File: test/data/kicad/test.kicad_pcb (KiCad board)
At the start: 2 copper layers, 101.6 x 53.3 mm, 64 parts, among them IC2 ATMEGA1280-16AU, IC4 MC33269D-5.0, IC6 FT232RL, IC7 LM358D, Q2 16MHz, T1 NDT2955, X2 DC21MMX

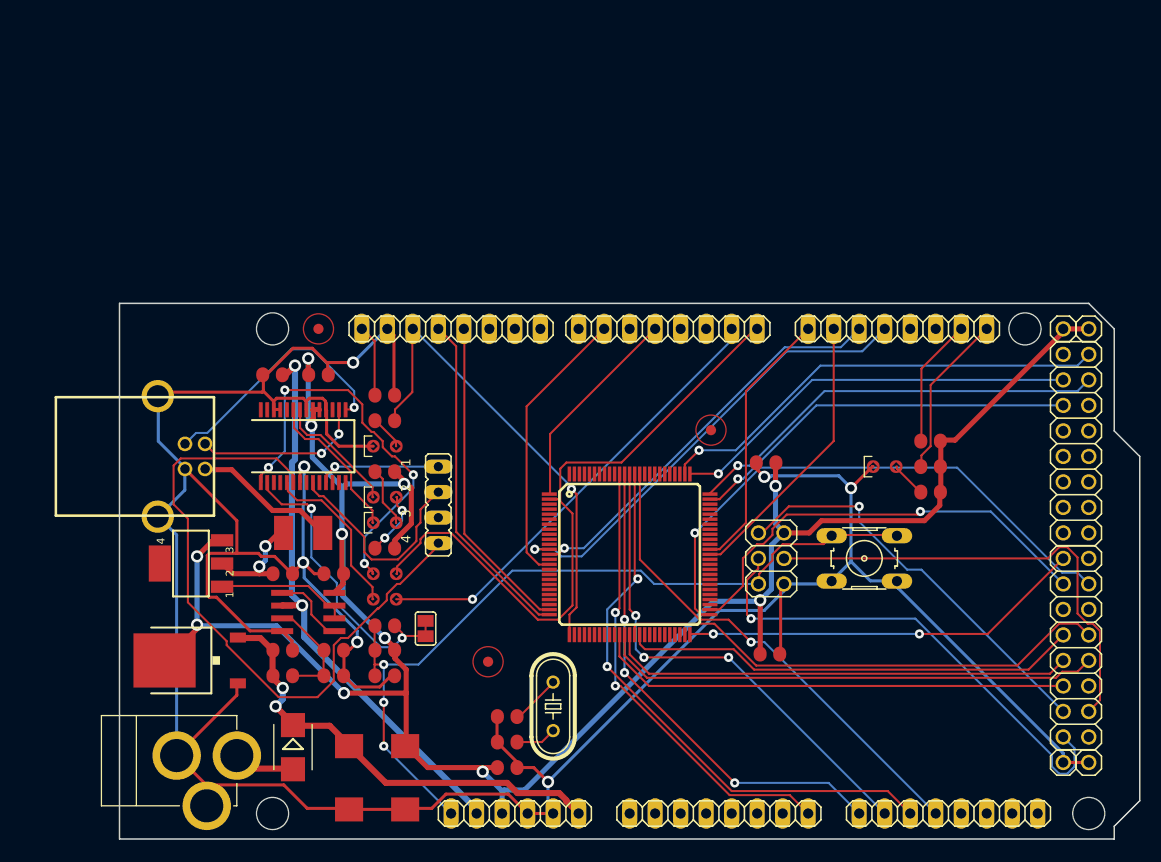
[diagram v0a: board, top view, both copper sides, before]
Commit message: rftr: kicad parser
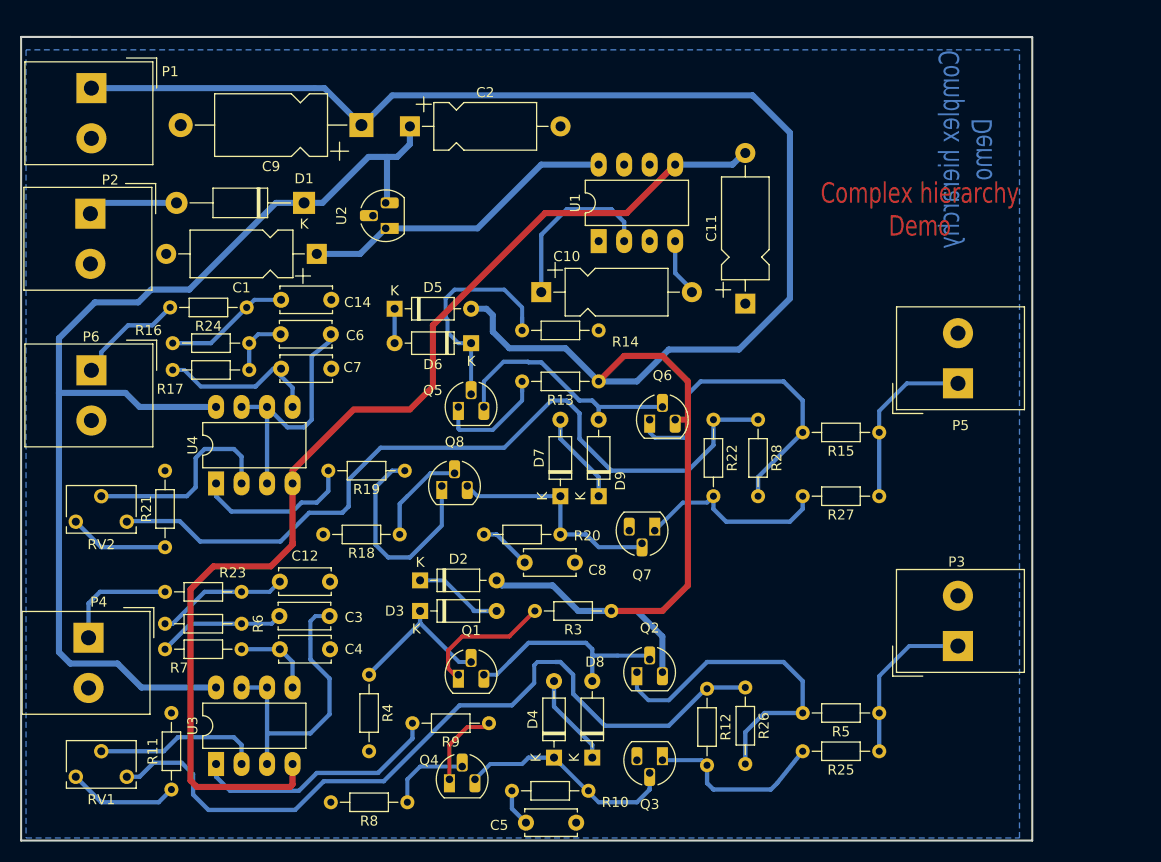
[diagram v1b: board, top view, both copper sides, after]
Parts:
- removed @HOLE0, @HOLE1, @HOLE2, @HOLE3: , 
- removed ADCH, ADCL, COMMUNICATION, PWMH, PWML: , 1X08
- removed C13, C15, C16, C17: 100n, C0805RND
- removed F1: 500mA, L1812
- removed IC2: ATMEGA1280-16AU, TQFP100
- removed IC4: MC33269D-5.0, DPACK
- removed IC6: FT232RL, SSOP28
- removed IC7: LM358D, SO08
- removed ICSP: ICSP, 2X03
- removed JP1, JP2: , 2X08
- removed JP3, JP4, JP5, JP6: , 1X01
- removed L, PWR, RX, TX: , 0805RND
- removed POWER: , 1X06
- removed R1: 1K, R0805RND
- removed R2: 10k, R0805RND
- removed RESET-EN: , SJ
- removed S1: , B3F-10XX
- removed T1: NDT2955, SOT223
- removed U$1, U$2, U$3: FIDUCIALMOUNT, FIDUCIA-MOUNT
- removed X2: DC21MMX, DC-21MM
- removed X3: , JP4
- removed X4: , PN61729
- added C8: 820pF, Capacitor_THT:C_Disc_D5.0mm_W2.5mm_P5.00mm, F.Cu at (138.0, 104.1)
- added D2: 1N4148, Diode_THT:D_DO-35_SOD27_P7.62mm_Horizontal, F.Cu at (127.6, 105.9)
- added D3: 1N4148, Diode_THT:D_DO-35_SOD27_P7.62mm_Horizontal, F.Cu at (127.6, 109.0)
- added D4: 1N4148, Diode_THT:D_DO-35_SOD27_P7.62mm_Horizontal, F.Cu at (141.0, 123.6)
- added D5: 1N4148, Diode_THT:D_DO-35_SOD27_P7.62mm_Horizontal, F.Cu at (125.1, 78.9)
- added D6: 1N4148, Diode_THT:D_DO-35_SOD27_P7.62mm_Horizontal, F.Cu at (132.7, 82.3)
- added D7: 1N4148, Diode_THT:D_DO-35_SOD27_P7.62mm_Horizontal, F.Cu at (141.6, 97.5)
- added D8: 1N4148, Diode_THT:D_DO-35_SOD27_P7.62mm_Horizontal, F.Cu at (144.8, 123.6)
- added D9: 1N4148, Diode_THT:D_DO-35_SOD27_P7.62mm_Horizontal, F.Cu at (145.4, 97.5)
- added P1: CONN_2, TerminalBlock_Altech:Altech_AK300_1x02_P5.00mm_45-Degree, F.Cu at (94.9, 56.9)
- added P2: CONN_2, TerminalBlock_Altech:Altech_AK300_1x02_P5.00mm_45-Degree, F.Cu at (94.8, 69.4)
- added P3: CONN_2, TerminalBlock_Altech:Altech_AK300_1x02_P5.00mm_45-Degree, F.Cu at (181.2, 112.5)
- added P4: CONN_2, TerminalBlock_Altech:Altech_AK300_1x02_P5.00mm_45-Degree, F.Cu at (94.6, 111.6)
- added P5: CONN_2, TerminalBlock_Altech:Altech_AK300_1x02_P5.00mm_45-Degree, F.Cu at (181.2, 86.3)
- added P6: CONN_2, TerminalBlock_Altech:Altech_AK300_1x02_P5.00mm_45-Degree, F.Cu at (94.9, 85.0)
- added Q1: MPSA92, Package_TO_SOT_THT:TO-92_HandSolder, F.Cu at (131.4, 115.3)
- added Q3: MPSA92, Package_TO_SOT_THT:TO-92_HandSolder, F.Cu at (151.8, 123.8)
- added Q4: MPSA42, Package_TO_SOT_THT:TO-92_HandSolder, F.Cu at (130.6, 125.7)
- added Q5: MPSA92, Package_TO_SOT_THT:TO-92_HandSolder, F.Cu at (131.4, 88.6)
- added Q6: MPSA42, Package_TO_SOT_THT:TO-92_HandSolder, F.Cu at (150.5, 89.9)
- added Q7: MPSA92, Package_TO_SOT_THT:TO-92_HandSolder, F.Cu at (151.0, 101.0)
- added Q8: MPSA42, Package_TO_SOT_THT:TO-92_HandSolder, F.Cu at (129.8, 96.5)
- added R13: 470, Resistor_THT:R_Axial_DIN0204_L3.6mm_D1.6mm_P7.62mm_Horizontal, F.Cu at (145.4, 86.1)
- added R14: 220K, Resistor_THT:R_Axial_DIN0204_L3.6mm_D1.6mm_P7.62mm_Horizontal, F.Cu at (137.8, 81.0)
- added R15: 47, Resistor_THT:R_Axial_DIN0204_L3.6mm_D1.6mm_P7.62mm_Horizontal, F.Cu at (173.4, 91.2)
- added R16: 22K, Resistor_THT:R_Axial_DIN0204_L3.6mm_D1.6mm_P7.62mm_Horizontal, F.Cu at (110.6, 82.3)
- added R17: 22K, Resistor_THT:R_Axial_DIN0204_L3.6mm_D1.6mm_P7.62mm_Horizontal, F.Cu at (103.0, 85.0)
- added R18: 1K, Resistor_THT:R_Axial_DIN0204_L3.6mm_D1.6mm_P7.62mm_Horizontal, F.Cu at (125.6, 101.3)
- added R19: 1K, Resistor_THT:R_Axial_DIN0204_L3.6mm_D1.6mm_P7.62mm_Horizontal, F.Cu at (126.1, 95.0)
- added R20: 5,6K, Resistor_THT:R_Axial_DIN0204_L3.6mm_D1.6mm_P7.62mm_Horizontal, F.Cu at (141.6, 101.3)
- added R21: 4,7K, Resistor_THT:R_Axial_DIN0204_L3.6mm_D1.6mm_P7.62mm_Horizontal, F.Cu at (102.2, 102.6)
- added R22: 220K, Resistor_THT:R_Axial_DIN0204_L3.6mm_D1.6mm_P7.62mm_Horizontal, F.Cu at (156.8, 89.9)
- added R23: 1K, Resistor_THT:R_Axial_DIN0204_L3.6mm_D1.6mm_P7.62mm_Horizontal, F.Cu at (109.9, 107.1)
- added R24: 1K, Resistor_THT:R_Axial_DIN0204_L3.6mm_D1.6mm_P7.62mm_Horizontal, F.Cu at (110.4, 78.7)
- added R25: 47, Resistor_THT:R_Axial_DIN0204_L3.6mm_D1.6mm_P7.62mm_Horizontal, F.Cu at (173.4, 122.9)
- added R26: 220K, Resistor_THT:R_Axial_DIN0204_L3.6mm_D1.6mm_P7.62mm_Horizontal, F.Cu at (160.0, 116.6)
- added R27: 47, Resistor_THT:R_Axial_DIN0204_L3.6mm_D1.6mm_P7.62mm_Horizontal, F.Cu at (173.4, 97.5)
- added R28: 220K, Resistor_THT:R_Axial_DIN0204_L3.6mm_D1.6mm_P7.62mm_Horizontal, F.Cu at (161.3, 89.9)
- added R4: 220K, Resistor_THT:R_Axial_DIN0204_L3.6mm_D1.6mm_P7.62mm_Horizontal, F.Cu at (122.6, 115.3)
- added RV1: 4,7K, Potentiometer_THT:Potentiometer_Bourns_3266W_Vertical, F.Cu at (93.3, 125.5)
- added RV2: 4,7K, Potentiometer_THT:Potentiometer_Bourns_3266W_Vertical, F.Cu at (93.3, 100.1)
- added U1: ICL7660, Package_DIP:DIP-8_W7.62mm_LongPads, F.Cu at (145.4, 72.1)
- added U2: 78L05, Package_TO_SOT_THT:TO-92_HandSolder, F.Cu at (124.2, 70.9)
- added U3: LM358N, Package_DIP:DIP-8_W7.62mm_LongPads, F.Cu at (107.3, 124.2)
- added U4: LM358N, Package_DIP:DIP-8_W7.62mm_LongPads, F.Cu at (107.3, 96.3)
- C1: value 100n -> 47uF; footprint C0805RND -> Capacitor_THT:CP_Axial_L10.0mm_D4.5mm_P15.00mm_Horizontal
- C10: value 100n -> 10uF; footprint C0805RND -> Capacitor_THT:CP_Axial_L10.0mm_D4.5mm_P15.00mm_Horizontal
- C11: value 22p -> 10uF; footprint C0805RND -> Capacitor_THT:CP_Axial_L10.0mm_D4.5mm_P15.00mm_Horizontal
- C12, C14: value 100n -> 150nF; footprint C0805RND -> Capacitor_THT:C_Disc_D5.0mm_W2.5mm_P5.00mm
- C2: value 22p -> 47uF/20V; footprint C0805RND -> Capacitor_THT:CP_Axial_L10.0mm_D4.5mm_P15.00mm_Horizontal
- C3: value 22p -> 15nF; footprint C0805RND -> Capacitor_THT:C_Disc_D5.0mm_W2.5mm_P5.00mm
- C4: value 100n -> 4.7nF; footprint C0805RND -> Capacitor_THT:C_Disc_D5.0mm_W2.5mm_P5.00mm
- C5: value 100n -> 820pF; footprint C0805RND -> Capacitor_THT:C_Disc_D5.0mm_W2.5mm_P5.00mm
- C6: value 100u -> 15nF; footprint SMC_D -> Capacitor_THT:C_Disc_D5.0mm_W2.5mm_P5.00mm
- C7: value 100u -> 4.7nF; footprint SMC_D -> Capacitor_THT:C_Disc_D5.0mm_W2.5mm_P5.00mm
- C9: value 100n -> 47uF/63V; footprint C0805RND -> Capacitor_THT:CP_Axial_L11.0mm_D6.0mm_P18.00mm_Horizontal
- D1: value (none) -> 1N4007; footprint SMB -> Diode_THT:D_DO-41_SOD81_P12.70mm_Horizontal
- Q2: value 16MHz -> MPSA42; footprint HC49_S -> Package_TO_SOT_THT:TO-92_HandSolder
- R10: value 10k -> 5,6K; footprint R0805RND -> Resistor_THT:R_Axial_DIN0204_L3.6mm_D1.6mm_P7.62mm_Horizontal
- R11: value 1K -> 4,7K; footprint RCL_0805RND -> Resistor_THT:R_Axial_DIN0204_L3.6mm_D1.6mm_P7.62mm_Horizontal
- R12: value 1K -> 220K; footprint RCL_0805RND -> Resistor_THT:R_Axial_DIN0204_L3.6mm_D1.6mm_P7.62mm_Horizontal
- R3: value 10k -> 470; footprint R0805RND -> Resistor_THT:R_Axial_DIN0204_L3.6mm_D1.6mm_P7.62mm_Horizontal
- R5: value 10K -> 47; footprint R0805RND -> Resistor_THT:R_Axial_DIN0204_L3.6mm_D1.6mm_P7.62mm_Horizontal
- R6: value 10k -> 22K; footprint R0805RND -> Resistor_THT:R_Axial_DIN0204_L3.6mm_D1.6mm_P7.62mm_Horizontal
- R7: value 1k -> 22K; footprint R0805RND -> Resistor_THT:R_Axial_DIN0204_L3.6mm_D1.6mm_P7.62mm_Horizontal
- R8: footprint R0805RND -> Resistor_THT:R_Axial_DIN0204_L3.6mm_D1.6mm_P7.62mm_Horizontal
- R9: value 1k -> 1K; footprint R0805RND -> Resistor_THT:R_Axial_DIN0204_L3.6mm_D1.6mm_P7.62mm_Horizontal
- moved C2 62.1 mm to (126.6, 60.7)
- moved R8 60.6 mm to (126.4, 128.0)
- moved C1 60.2 mm to (117.3, 73.4), turned to 180 degrees
- moved D1 54.2 mm to (116.1, 68.3), turned to 180 degrees
- moved C9 52.5 mm to (121.8, 60.6)
- moved C11 51.6 mm to (160.0, 78.4), turned to 90 degrees
- moved R5 49.6 mm to (173.4, 119.1), turned to 180 degrees
- moved C10 47.5 mm to (139.7, 77.2)
- moved C6 44.2 mm to (118.7, 81.4), turned to 180 degrees
- moved C7 42.6 mm to (113.8, 84.8), turned to 0 degrees
- moved R3 36.0 mm to (146.7, 109.0)
- moved R12 33.3 mm to (156.2, 116.7), turned to -90 degrees
- moved R10 32.5 mm to (144.4, 126.9)
- moved R11 30.2 mm to (102.9, 126.7), turned to 90 degrees
- moved C5 29.7 mm to (138.2, 130.0)
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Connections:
- C1 pad 1: +5V -> VCC
- C10 pad 1: +5V -> Net-(U1-CAP+)
- C10 pad 2: GND -> Net-(U1-CAP-)
- C11 pad 1: RESET -> GND
- C11 pad 2: GND -> -VAA
- C12 pad 1: DTR -> Net-(C12-Pad1)
- C12 pad 2: RESET -> GND
- C14 pad 1: USBVCC -> Net-(C14-Pad1)
- C2 pad 1: GND -> +12V
- C2 pad 2: N$6 -> GND
- C3 pad 1: GND -> /ampli_ht_vertical/Vpil_0_3,3V
- C3 pad 2: N$7 -> Net-(C3-Pad2)
- C4 pad 1: AREF -> Net-(U3B-+)
- C5 pad 1: VIN -> Net-(C5-Pad1)
- C9 pad 1: +5V -> HT
- Q2 pad 1: N$6 -> Net-(Q2-E)
- Q2 pad 2: N$7 -> Net-(D8-A)
- R10 pad 1: CMP -> Net-(D4-K)
- R10 pad 2: VIN -> Net-(C5-Pad1)
- R3 pad 1: +5V -> HT
- R3 pad 2: SDA -> Net-(Q1-E)
- R5 pad 1: RESET -> /ampli_ht_vertical/PIEZO_OUT
- R5 pad 2: +5V -> Net-(Q2-E)
- R6 pad 1: GND -> Net-(C3-Pad2)
- R6 pad 2: CMP -> Net-(C12-Pad1)
- R7 pad 1: N$54 -> Net-(U3B-+)
- R7 pad 2: +5V -> Net-(C3-Pad2)
- R8 pad 1: +5V -> Net-(Q4-B)
- R8 pad 2: N$3 -> GND
- R9 pad 2: +5V -> Net-(R9-Pad2)
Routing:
- net GND: track 333.2 -> 0.00 mm, vias 7 -> 0
- net +5V: track 219.3 -> 0.00 mm, vias 11 -> 0
- net HT: track 0.00 -> 193.2 mm
- net +12V: track 0.00 -> 114.0 mm
- net -VAA: track 0.00 -> 112.8 mm
- net RESET: track 82.3 -> 0.00 mm, vias 3 -> 0
- net /ampli_ht_horizontal/S_OUT+: track 0.00 -> 79.2 mm
- net /ampli_ht_vertical/S_OUT+: track 0.00 -> 77.8 mm
- net RI: track 65.9 -> 0.00 mm
- net PE0: track 64.7 -> 0.00 mm
- net ADC10: track 56.8 -> 0.00 mm, vias 2 -> 0
- net +3V3: track 56.0 -> 0.00 mm, vias 2 -> 0
- net PG0: track 56.0 -> 0.00 mm, vias 1 -> 0
- net PL4: track 50.1 -> 0.00 mm
- net PL2: track 49.9 -> 0.00 mm
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- added copper zone on B.Cu, net GND
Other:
- board size 101.6 x 53.3 mm -> 100.7 x 80 mm
- net class Default removed
- rule pad_to_mask_clearance: 0.051 -> 0
- board text added: "Complex hierarchy Demo"
